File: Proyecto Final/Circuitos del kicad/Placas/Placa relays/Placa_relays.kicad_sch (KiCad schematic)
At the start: 47 parts, among them J1 12v, J4 Conn_01x08, J5 Conn_01x08, J6 Conn_01x06, Q1 PN2222A, Q2 PN2222A, Q3 PN2222A, SW1 SW_Push, SW2 SW_Push, SW3 SW_Push, SW4 SW_Push, U1 LM7805, U2 ESP-12E, U3 ATmega328P-P, U4 LM1117-3.3, U5 BOB-12009, Y1 16MHz

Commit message: Cambios placa relays
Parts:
- removed C1, C2: 20pF, Capacitor_THT:C_Disc_D5.0mm_W2.5mm_P5.00mm, symbol Device:C
- removed C3: 330nF, Capacitor_THT:C_Disc_D5.0mm_W2.5mm_P5.00mm, symbol Device:C
- removed C4, C5: 100nF, Capacitor_THT:C_Disc_D5.0mm_W2.5mm_P5.00mm, symbol Device:C
- removed C6: 10uF, Capacitor_THT:C_Disc_D5.0mm_W2.5mm_P5.00mm, symbol Device:C
- removed Encoder/puls-arduino1: Conn_02x06_Odd_Even, ENCODER+PULS:ENCODER+PULS_arduino, symbol ENCODER+PULS_arduino:Conn_02x06_Odd_Even
- removed Encoder/puls2: Conn_02x06_Odd_Even, ENCODER+PULS:ENCODER+PULS, symbol ENCODER+PULS:Conn_02x06_Odd_Even
- removed Encoder1: Conn_01x05, Connector_PinHeader_2.54mm:PinHeader_1x05_P2.54mm_Vertical, symbol Connector_Generic:Conn_01x05
- removed J1: 12v, TerminalBlock:TerminalBlock_bornier-2_P5.08mm, symbol Connector_Generic:Conn_01x02
- removed J4, J5: Conn_01x08, Connector_PinHeader_2.54mm:PinHeader_1x08_P2.54mm_Vertical, symbol Connector_Generic:Conn_01x08
- removed J6: Conn_01x06, Connector_PinHeader_2.54mm:PinHeader_1x06_P2.54mm_Vertical, symbol Connector_Generic:Conn_01x06
- removed R1: 4.7k, Resistor_THT:R_Axial_DIN0204_L3.6mm_D1.6mm_P5.08mm_Horizontal, symbol Device:R_Small_US
- removed R7, R8: 10k, Resistor_THT:R_Axial_DIN0204_L3.6mm_D1.6mm_P5.08mm_Horizontal, symbol Device:R
- removed RTC+LCD1: Conn_02x04_Odd_Even, Connector_PinHeader_2.54mm:PinHeader_2x04_P2.54mm_Vertical, symbol Connector_Generic:Conn_02x04_Odd_Even
- removed Relay+DS18B20+LVL_SENS1: Conn_02x05_Odd_Even_1, RELAY+DS18B20+LVLSENS:RELAY+DS18B20+LVLSENS, symbol RELAY+DS18B20+LVLSENS:Conn_02x05_Odd_Even_1
- removed Relay1: Conn_02x05_Odd_Even, RELAY+DS18B20+LVLSENS:ENCODER+PULS_PLACA_SALIDAS, symbol RELAY+DS18B20+LVLSENS_PLACA_SALIDAS:Conn_02x05_Odd_Even
- removed SW1, SW2, SW3, SW4: SW_Push, Button_Switch_THT:SW_PUSH-12mm, symbol Switch:SW_Push
- removed U1: LM7805, Package_TO_SOT_THT:TO-220-3_Vertical, symbol Regulator_Linear:LM7805_TO220
- removed U2: ESP-12E, ESP8266-12E_ESP-12E:XCVR_ESP8266-12E_ESP-12E, symbol ESP8266:ESP-12E
- removed U3: ATmega328P-P, Package_DIP:DIP-28_W7.62mm, symbol MCU_Microchip_ATmega:ATmega328P-P
- removed U4: LM1117-3.3, Package_TO_SOT_SMD:SOT-223, symbol Regulator_Linear:LM1117-3.3
- removed U5: BOB-12009, CONV_BOB-12009, symbol BOB-12009:BOB-12009
- removed Y1: 16MHz, Crystal:Crystal_HC49-4H_Vertical, symbol Device:Crystal
- added D4, D5, D6: LED, LED_THT:LED_D5.0mm, symbol Device:LED
- added J1: Conn_02x05_Odd_Even, Connector_IDC:IDC-Header_2x05_P2.54mm_Vertical, symbol Connector_Generic:Conn_02x05_Odd_Even
- added R1: 470, Resistor_THT:R_Axial_DIN0204_L3.6mm_D1.6mm_P5.08mm_Horizontal, symbol Device:R
- R5, R6: value 10k -> 470
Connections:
- net +12V: now also J1.10 (Pin_10)
- net +5V: now also J1.9 (Pin_9); no longer R5.2, R6.2
- net GND: now also D4.1 (K), D5.1 (K), D6.1 (K), J1.1 (Pin_1), J1.2 (Pin_2)
- net at D1.2 (A), Q3.3 (C), Relay-1.A2: now also R1.1
- net at D3.2 (A), Q1.3 (C), Relay-3.A2: now also R6.1
- net at R3.2: now also J1.4 (Pin_4)
- net at D2.2 (A), Q2.3 (C), Relay-2.A2: now also R5.1
- net at R2.2: now also J1.8 (Pin_8)
- net at Salidas_sensores1.3 (Pin_3): now also J1.5 (Pin_5)
- net at R4.2: now also J1.6 (Pin_6)
- net at Salidas_sensores1.2 (Pin_2): now also J1.7 (Pin_7)
- new net: D5.2 (A), R5.2
- new net: D4.2 (A), R1.2
- new net: D6.2 (A), R6.2
- no-connect marks 13 -> 4
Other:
- note removed: "RST"
- note removed: "RX"
- note removed: "TX"
- moved on the sheet: D1, D2, D3, Q1, Q2, Q3, R2, R3, R4, Relay-1, Relay-2, Relay-3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

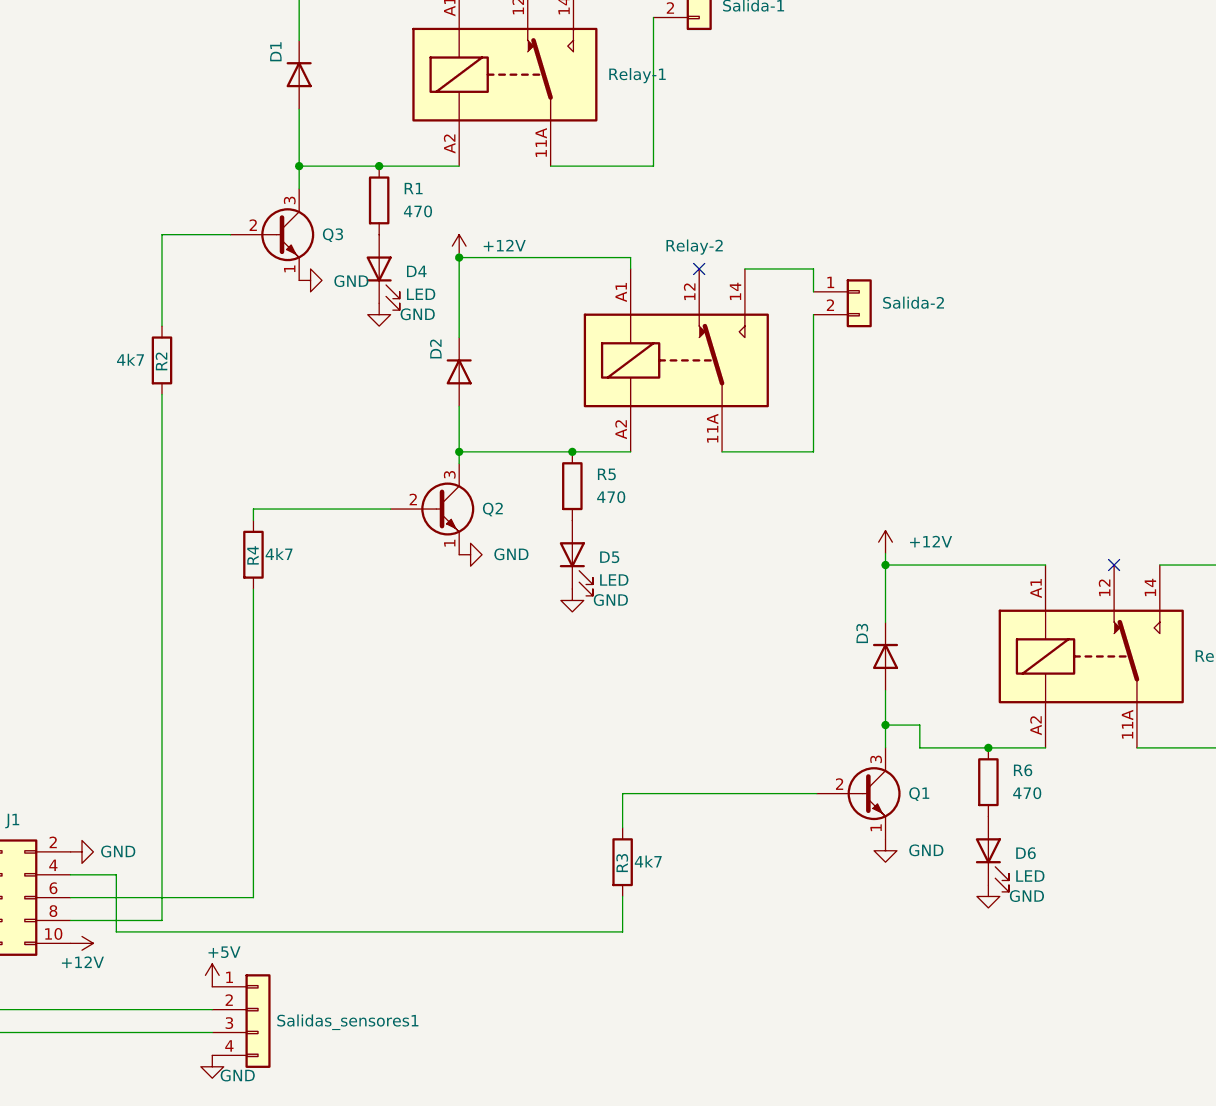
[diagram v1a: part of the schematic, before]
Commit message: Agregado placa todo en uno
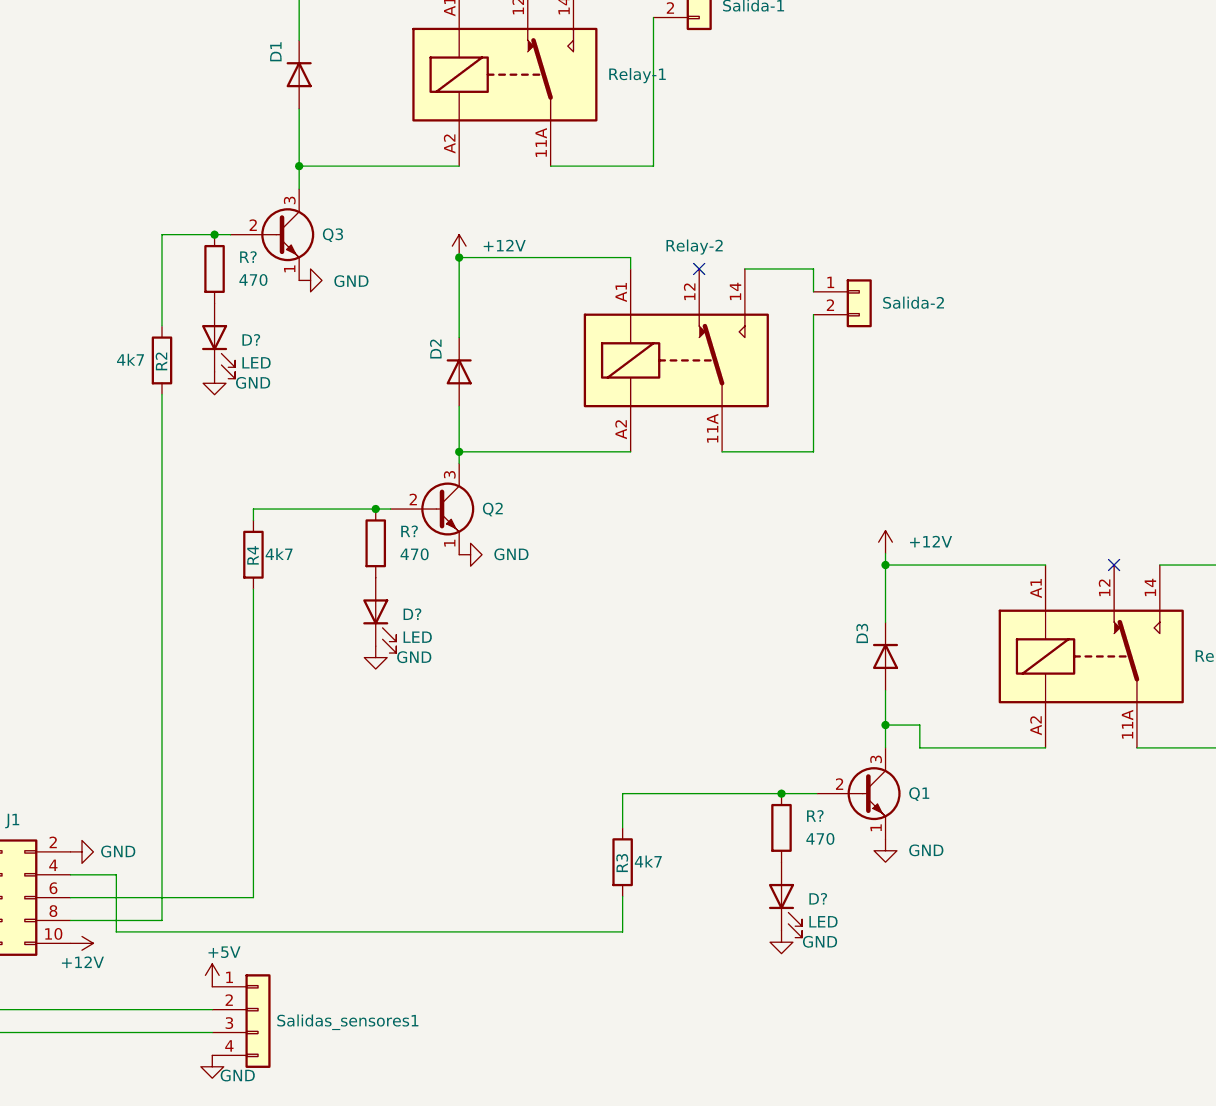
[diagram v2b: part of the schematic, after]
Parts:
- removed D4, D5, D6: LED, LED_THT:LED_D5.0mm, symbol Device:LED
- removed R1, R5, R6: 470, Resistor_THT:R_Axial_DIN0204_L3.6mm_D1.6mm_P5.08mm_Horizontal, symbol Device:R
- added D? (x3): LED, LED_THT:LED_D5.0mm, symbol Device:LED
- added R? (x3): 470, Resistor_THT:R_Axial_DIN0204_L3.6mm_D1.6mm_P5.08mm_Horizontal, symbol Device:R
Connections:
- net GND: now also D?.1 (K), D?.1 (K), D?.1 (K)
- net at Q1.2 (B), R3.1: now also R?.1
- net at Q3.2 (B), R2.1: now also R?.1
- net at Q2.2 (B), R4.1: now also R?.1
- new net: D?.2 (A), R?.2 (x3)

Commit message: wewew
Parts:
- R1, R5, R6: renamed from R?; footprint Resistor_THT:R_Axial_DIN0204_L3.6mm_D1.6mm_P5.08mm_Horizontal -> Resistor_THT:R_Axial_DIN0207_L6.3mm_D2.5mm_P7.62mm_Horizontal
- R2, R3, R4: footprint Resistor_THT:R_Axial_DIN0204_L3.6mm_D1.6mm_P7.62mm_Horizontal -> Resistor_THT:R_Axial_DIN0207_L6.3mm_D2.5mm_P7.62mm_Horizontal
- gave numbers to parts that had none: 3
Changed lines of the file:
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@@
       (effects (font (size 1.27 1.27)) (justify left))
     )
-    (property "Footprint" "Resistor_THT:R_Axial_DIN0204_L3.6mm_D1.6mm_P7.62mm_Horizontal" (id 2) (at 156.337 138.049 90)
+    (property "Footprint" "Resistor_THT:R_Axial_DIN0207_L6.3mm_D2.5mm_P7.62mm_Horizontal" (id 2) (at 156.337 138.049 90)
       (effects (font (size 1.27 1.27)) hide)
     )
@@
   (symbol (lib_id "Device:R") (at 112.776 72.136 0) (unit 1)
     (in_bom yes) (on_board yes) (fields_autoplaced)
-    (property "Reference" "R?" (id 0) (at 115.443 70.8659 0)
+    (property "Reference" "R1" (id 0) (at 115.443 70.8659 0)
       (effects (font (size 1.27 1.27)) (justify left))
     )
@@
       (effects (font (size 1.27 1.27)) (justify left))
     )
-    (property "Footprint" "Resistor_THT:R_Axial_DIN0204_L3.6mm_D1.6mm_P5.08mm_Horizontal" (id 2) (at 110.998 72.136 90)
+    (property "Footprint" "Resistor_THT:R_Axial_DIN0207_L6.3mm_D2.5mm_P7.62mm_Horizontal" (id 2) (at 110.998 72.136 90)
       (effects (font (size 1.27 1.27)) hide)
     )
@@
   (symbol (lib_id "power:GND") (at 175.768 145.669 0) (unit 1)
     (in_bom yes) (on_board yes) (fields_autoplaced)
-    (property "Reference" "#PWR?" (id 0) (at 175.768 152.019 0)
+    (property "Reference" "#PWR0103" (id 0) (at 175.768 152.019 0)
       (effects (font (size 1.27 1.27)) hide)
     )
@@
       (effects (font (size 1.27 1.27)) (justify left))
     )
-    (property "Footprint" "Resistor_THT:R_Axial_DIN0204_L3.6mm_D1.6mm_P7.62mm_Horizontal" (id 2) (at 105.156 82.296 90)
+    (property "Footprint" "Resistor_THT:R_Axial_DIN0207_L6.3mm_D2.5mm_P7.62mm_Horizontal" (id 2) (at 105.156 82.296 90)
       (effects (font (size 1.27 1.27)) hide)
     )
@@
   (symbol (lib_id "power:GND") (at 112.776 83.566 0) (unit 1)
     (in_bom yes) (on_board yes) (fields_autoplaced)
-    (property "Reference" "#PWR?" (id 0) (at 112.776 89.916 0)
+    (property "Reference" "#PWR0104" (id 0) (at 112.776 89.916 0)
       (effects (font (size 1.27 1.27)) hide)
     )
@@
   (symbol (lib_id "Device:R") (at 175.768 134.239 0) (unit 1)
     (in_bom yes) (on_board yes) (fields_autoplaced)
-    (property "Reference" "R?" (id 0) (at 178.435 132.9689 0)
+    (property "Reference" "R6" (id 0) (at 178.435 132.9689 0)
       (effects (font (size 1.27 1.27)) (justify left))
     )
@@
       (effects (font (size 1.27 1.27)) (justify left))
     )
-    (property "Footprint" "Resistor_THT:R_Axial_DIN0204_L3.6mm_D1.6mm_P5.08mm_Horizontal" (id 2) (at 173.99 134.239 90)
+    (property "Footprint" "Resistor_THT:R_Axial_DIN0207_L6.3mm_D2.5mm_P7.62mm_Horizontal" (id 2) (at 173.99 134.239 90)
       (effects (font (size 1.27 1.27)) hide)
     )
@@
       (effects (font (size 1.27 1.27)) (justify left))
     )
-    (property "Footprint" "Resistor_THT:R_Axial_DIN0204_L3.6mm_D1.6mm_P7.62mm_Horizontal" (id 2) (at 115.316 103.886 90)
+    (property "Footprint" "Resistor_THT:R_Axial_DIN0207_L6.3mm_D2.5mm_P7.62mm_Horizontal" (id 2) (at 115.316 103.886 90)
       (effects (font (size 1.27 1.27)) hide)
     )
@@
   (symbol (lib_id "Device:LED") (at 175.768 141.859 90) (unit 1)
     (in_bom yes) (on_board yes) (fields_autoplaced)
-    (property "Reference" "D?" (id 0) (at 178.689 142.1764 90)
+    (property "Reference" "D6" (id 0) (at 178.689 142.1764 90)
       (effects (font (size 1.27 1.27)) (justify right))
     )
@@
   (symbol (lib_id "Device:R") (at 130.683 102.616 0) (unit 1)
     (in_bom yes) (on_board yes) (fields_autoplaced)
-    (property "Reference" "R?" (id 0) (at 133.35 101.3459 0)
+    (property "Reference" "R5" (id 0) (at 133.35 101.3459 0)
       (effects (font (size 1.27 1.27)) (justify left))
     )
@@
       (effects (font (size 1.27 1.27)) (justify left))
     )
-    (property "Footprint" "Resistor_THT:R_Axial_DIN0204_L3.6mm_D1.6mm_P5.08mm_Horizontal" (id 2) (at 128.905 102.616 90)
+    (property "Footprint" "Resistor_THT:R_Axial_DIN0207_L6.3mm_D2.5mm_P7.62mm_Horizontal" (id 2) (at 128.905 102.616 90)
       (effects (font (size 1.27 1.27)) hide)
     )
@@
   (symbol (lib_id "Device:LED") (at 112.776 79.756 90) (unit 1)
     (in_bom yes) (on_board yes) (fields_autoplaced)
-    (property "Reference" "D?" (id 0) (at 115.697 80.0734 90)
+    (property "Reference" "D4" (id 0) (at 115.697 80.0734 90)
       (effects (font (size 1.27 1.27)) (justify right))
     )
@@
   (symbol (lib_id "power:GND") (at 130.683 114.046 0) (unit 1)
     (in_bom yes) (on_board yes) (fields_autoplaced)
-    (property "Reference" "#PWR?" (id 0) (at 130.683 120.396 0)
+    (property "Reference" "#PWR0101" (id 0) (at 130.683 120.396 0)
       (effects (font (size 1.27 1.27)) hide)
     )
@@
   (symbol (lib_id "Device:LED") (at 130.683 110.236 90) (unit 1)
     (in_bom yes) (on_board yes) (fields_autoplaced)
-    (property "Reference" "D?" (id 0) (at 133.604 110.5534 90)
+    (property "Reference" "D5" (id 0) (at 133.604 110.5534 90)
       (effects (font (size 1.27 1.27)) (justify right))
     )
@@
       (reference "#PWR011") (unit 1) (value "+12V") (footprint "")
     )
+    (path "/c1489a3b-31cc-4abc-b831-deb2ef15aecb"
+      (reference "#PWR0101") (unit 1) (value "GND") (footprint "")
+    )
     (path "/0ffdb656-74ac-4f5f-8d35-f8e3ed888b9b"
       (reference "#PWR0102") (unit 1) (value "+5V") (footprint "")
     )
+    (path "/38ed4391-3bd5-4c59-8de0-2d916778d345"
+      (reference "#PWR0103") (unit 1) (value "GND") (footprint "")
+    )
+    (path "/51e9ff4f-6264-447d-b852-8d3204f9364e"
+      (reference "#PWR0104") (unit 1) (value "GND") (footprint "")
+    )
     (path "/2a8784e8-ea9b-4fda-b107-08ff0ad6a443"
       (reference "#PWR0107") (unit 1) (value "GND") (footprint "")
@@
       (reference "#PWR0140") (unit 1) (value "GND") (footprint "")
     )
-    (path "/38ed4391-3bd5-4c59-8de0-2d916778d345"
-      (reference "#PWR?") (unit 1) (value "GND") (footprint "")
-    )
-    (path "/51e9ff4f-6264-447d-b852-8d3204f9364e"
-      (reference "#PWR?") (unit 1) (value "GND") (footprint "")
-    )
-    (path "/c1489a3b-31cc-4abc-b831-deb2ef15aecb"
-      (reference "#PWR?") (unit 1) (value "GND") (footprint "")
-    )
     (path "/08bf3937-4a24-4eec-bd98-355db579b426"
       (reference "D1") (unit 1) (value "1N4007") (footprint "Diode_THT:D_DO-41_SOD81_P10.16mm_Horizontal")
@@
       (reference "D3") (unit 1) (value "1N4007") (footprint "Diode_THT:D_DO-41_SOD81_P10.16mm_Horizontal")
     )
+    (path "/b00c5c4b-78cb-4f9d-9797-5338adb371ee"
+      (reference "D4") (unit 1) (value "LED") (footprint "LED_THT:LED_D5.0mm")
+    )
+    (path "/eebcad0e-49b2-4281-aa81-6da8a66565c1"
+      (reference "D5") (unit 1) (value "LED") (footprint "LED_THT:LED_D5.0mm")
+    )
     (path "/757ebd53-451f-4643-b312-fd0eea8ef01b"
-      (reference "D?") (unit 1) (value "LED") (footprint "LED_THT:LED_D5.0mm")
-    )
-    (path "/b00c5c4b-78cb-4f9d-9797-5338adb371ee"
-      (reference "D?") (unit 1) (value "LED") (footprint "LED_THT:LED_D5.0mm")
-    )
-    (path "/eebcad0e-49b2-4281-aa81-6da8a66565c1"
-      (reference "D?") (unit 1) (value "LED") (footprint "LED_THT:LED_D5.0mm")
+      (reference "D6") (unit 1) (value "LED") (footprint "LED_THT:LED_D5.0mm")
     )
     (path "/25109542-1f02-499f-ac1d-b082ae157bb2"
@@
       (reference "Q3") (unit 1) (value "PN2222A") (footprint "Package_TO_SOT_THT:TO-92_Inline")
     )
+    (path "/29f0e40b-d0ea-40e0-9137-fc6d3b191996"
+      (reference "R1") (unit 1) (value "470") (footprint "Resistor_THT:R_Axial_DIN0207_L6.3mm_D2.5mm_P7.62mm_Horizontal")
+    )
     (path "/3f4175bd-b531-4d70-acca-18a347e25b40"
-      (reference "R2") (unit 1) (value "4k7") (footprint "Resistor_THT:R_Axial_DIN0204_L3.6mm_D1.6mm_P7.62mm_Horizontal")
+      (reference "R2") (unit 1) (value "4k7") (footprint "Resistor_THT:R_Axial_DIN0207_L6.3mm_D2.5mm_P7.62mm_Horizontal")
     )
     (path "/28062e64-1181-48d2-bf21-6f78b83b1a49"
-      (reference "R3") (unit 1) (value "4k7") (footprint "Resistor_THT:R_Axial_DIN0204_L3.6mm_D1.6mm_P7.62mm_Horizontal")
+      (reference "R3") (unit 1) (value "4k7") (footprint "Resistor_THT:R_Axial_DIN0207_L6.3mm_D2.5mm_P7.62mm_Horizontal")
     )
     (path "/67eb0b79-23ed-43e5-b8ab-6b20e939ccbf"
-      (reference "R4") (unit 1) (value "4k7") (footprint "Resistor_THT:R_Axial_DIN0204_L3.6mm_D1.6mm_P7.62mm_Horizontal")
-    )
-    (path "/29f0e40b-d0ea-40e0-9137-fc6d3b191996"
-      (reference "R?") (unit 1) (value "470") (footprint "Resistor_THT:R_Axial_DIN0204_L3.6mm_D1.6mm_P5.08mm_Horizontal")
+      (reference "R4") (unit 1) (value "4k7") (footprint "Resistor_THT:R_Axial_DIN0207_L6.3mm_D2.5mm_P7.62mm_Horizontal")
+    )
+    (path "/9b0a4741-5862-4126-992f-cff362b17a36"
+      (reference "R5") (unit 1) (value "470") (footprint "Resistor_THT:R_Axial_DIN0207_L6.3mm_D2.5mm_P7.62mm_Horizontal")
     )
     (path "/5dca0347-3136-4487-b4f0-affe67849308"
-      (reference "R?") (unit 1) (value "470") (footprint "Resistor_THT:R_Axial_DIN0204_L3.6mm_D1.6mm_P5.08mm_Horizontal")
-    )
-    (path "/9b0a4741-5862-4126-992f-cff362b17a36"
-      (reference "R?") (unit 1) (value "470") (footprint "Resistor_THT:R_Axial_DIN0204_L3.6mm_D1.6mm_P5.08mm_Horizontal")
+      (reference "R6") (unit 1) (value "470") (footprint "Resistor_THT:R_Axial_DIN0207_L6.3mm_D2.5mm_P7.62mm_Horizontal")
     )
     (path "/0cd577a2-42ef-4733-8afe-9d3894fc9450"
